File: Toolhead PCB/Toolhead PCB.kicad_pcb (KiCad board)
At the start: 2 copper layers, 35.7 x 22 mm, 9 parts, among them J1 PicoA, J2 PicoB, J3 PicoC, J4 Heater, J5 Thermistor, J6 Heatbreak Fan, J7 Part Fan, J8 IR+ADXL345, J9 MicroProbe

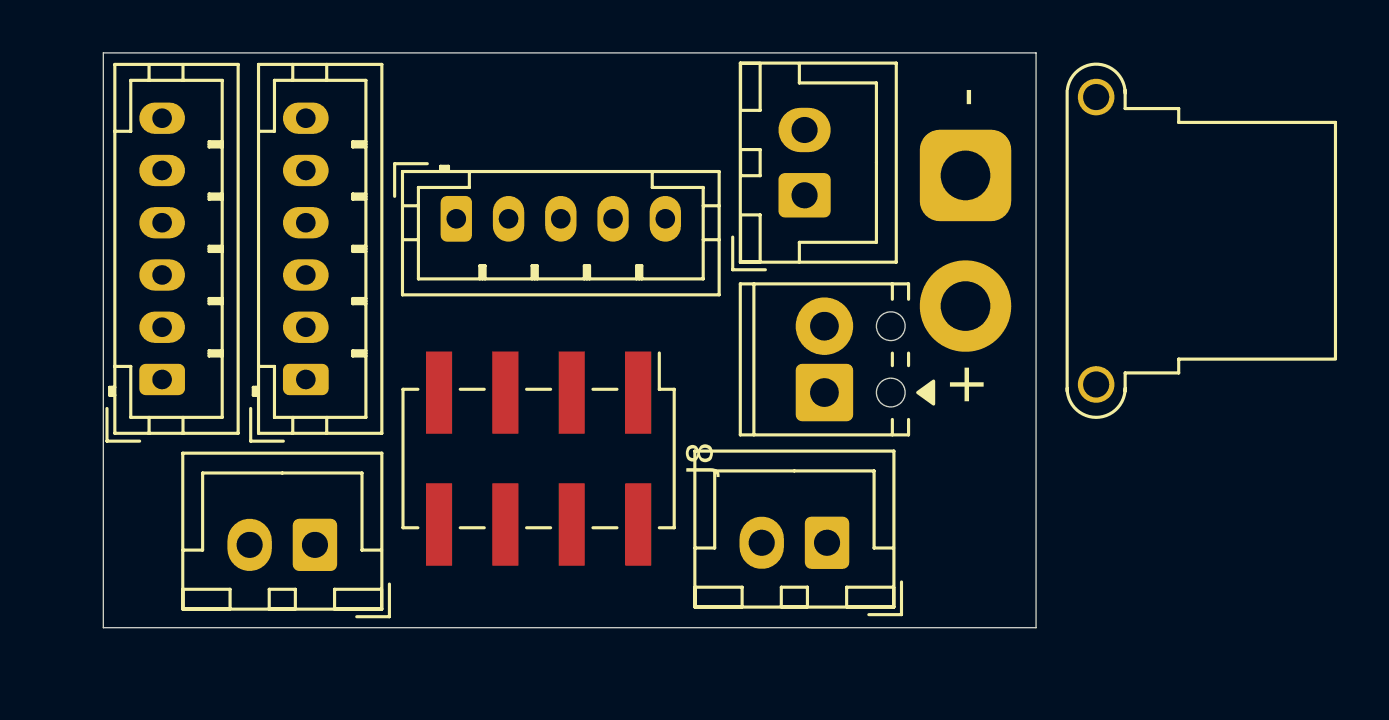
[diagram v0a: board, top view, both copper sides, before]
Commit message: Used wider traces for heater, fans, thermistor, microprobe power, etc.
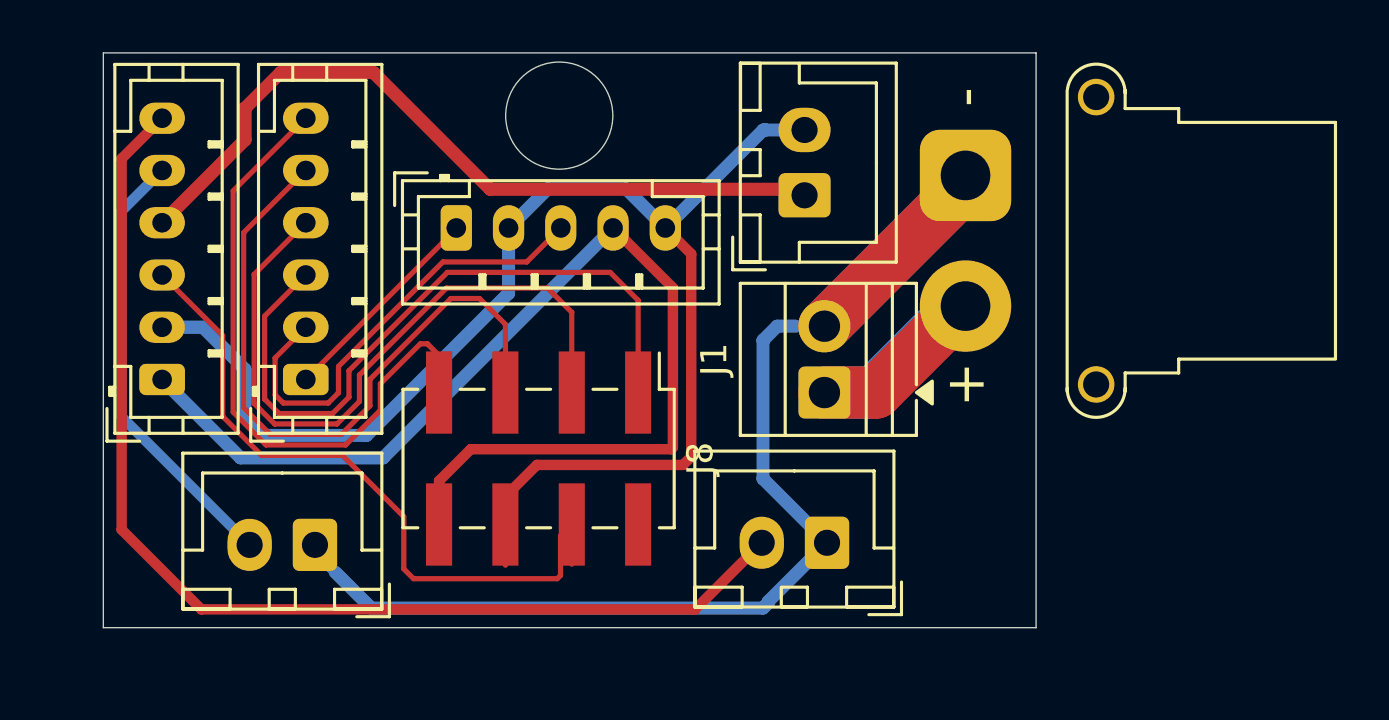
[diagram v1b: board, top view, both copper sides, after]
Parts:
- J1: footprint TerminalBlock_Phoenix:TerminalBlock_Phoenix_MPT-0,5-2-2.54_1x02_P2.54mm_Horizontal -> TerminalBlock:TerminalBlock_Xinya_XY308-2.54-2P_1x02_P2.54mm_Horizontal
- moved J9 0.35 mm to (113.5, 56.7)
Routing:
- net Net-(J3-Pin_2): track 0.00 -> 56.2 mm
- net Net-(J1-Pin_2): track 0.00 -> 53.3 mm
- net Net-(J3-Pin_6): track 0.00 -> 47.3 mm
- net Net-(J3-Pin_1): track 0.00 -> 43.0 mm
- net Net-(J3-Pin_4): track 0.00 -> 30.2 mm
- net Net-(J3-Pin_3): track 0.00 -> 26.8 mm
- net Net-(J2-Pin_3): track 0.00 -> 26.7 mm
- net Net-(J2-Pin_4): track 0.00 -> 26.4 mm
- net Net-(J2-Pin_5): track 0.00 -> 26.3 mm
- net Net-(J2-Pin_6): track 0.00 -> 24.6 mm
- net Net-(J2-Pin_2): track 0.00 -> 17.5 mm
- net Net-(J3-Pin_5): track 0.00 -> 17.0 mm
- net Net-(J1-Pin_1): track 0.00 -> 14.8 mm
- net Net-(J2-Pin_1): track 0.00 -> 8.19 mm
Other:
- outline, holes or cut-outs redrawn

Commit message: Combine a through-hole and an SMD connector to get the passthrough holes and vias.
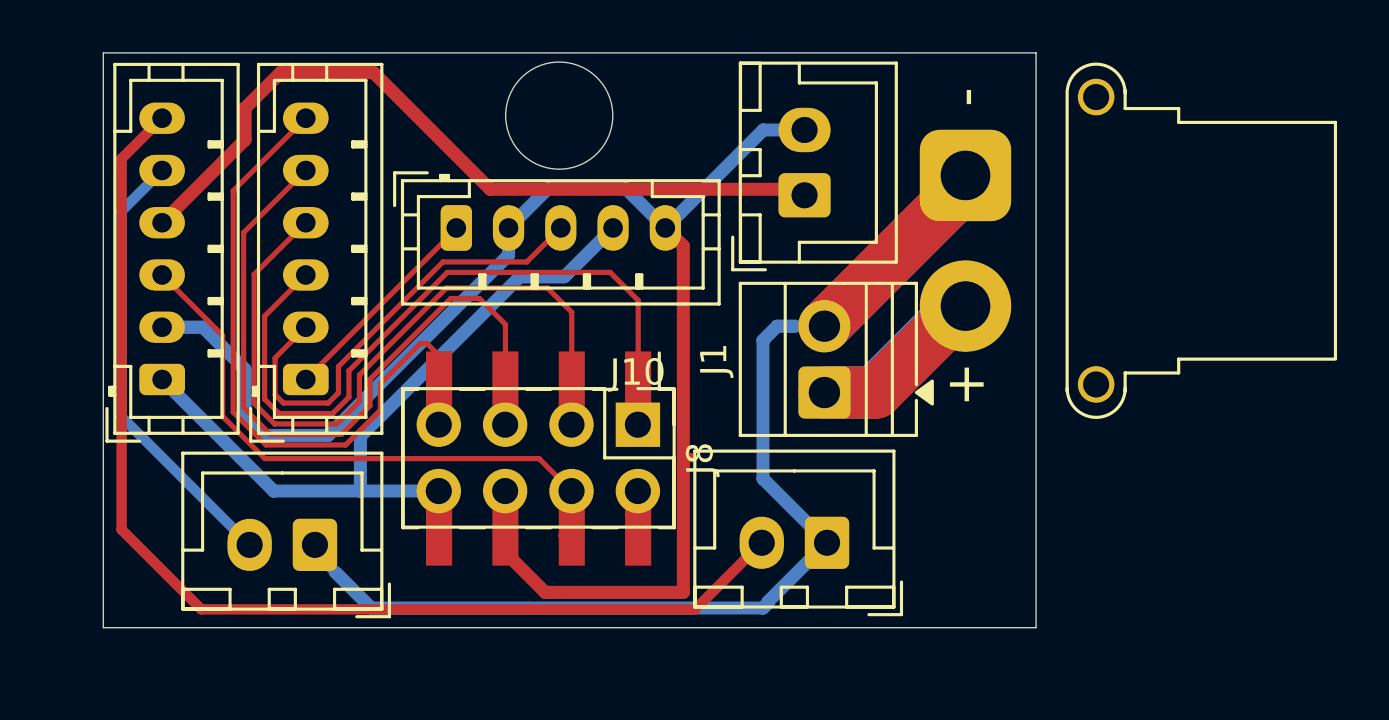
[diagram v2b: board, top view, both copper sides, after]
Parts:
- added J10: Conn_02x04_Odd_Even, Connector_PinHeader_2.54mm:PinHeader_2x04_P2.54mm_Vertical, F.Cu at (120.5, 64.2)
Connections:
- J8 pad 2: unconnected-(J8-Pin_2-Pad2) -> Net-(J10-Pin_2)
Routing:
- net Net-(J10-Pin_8): track 43.0 -> 30.0 mm
- net Net-(J10-Pin_4): track 26.8 -> 21.5 mm
- net Net-(J10-Pin_6): track 56.2 -> 59.2 mm

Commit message: JST connectors are soldered to the back: added 8 vias for signal and 2 vias for fan power. Added mounting holes (but have not resolved clearances).
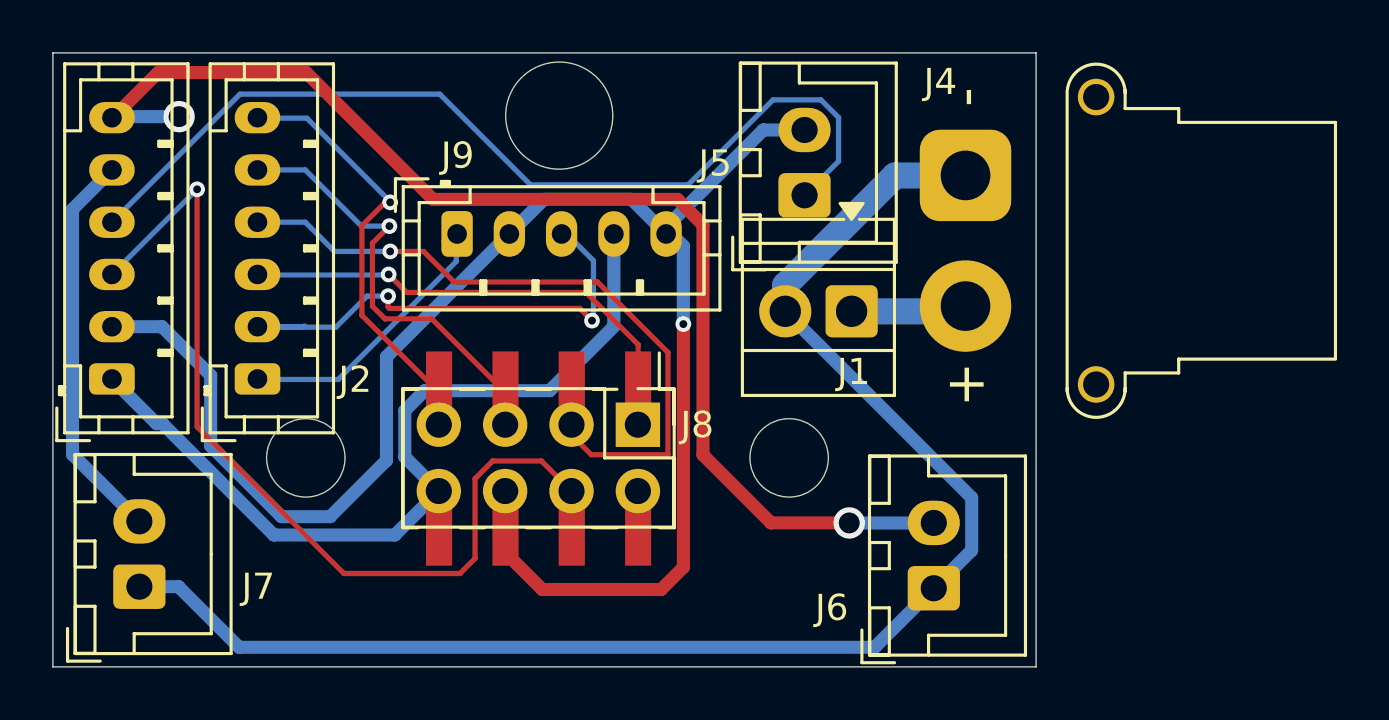
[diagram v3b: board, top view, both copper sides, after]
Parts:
- moved J7 6.91 mm to (101.4, 70.4), turned to 90 degrees
- moved J6 4.44 mm to (131.8, 70.5), turned to 90 degrees
- moved J1 3.28 mm to (128.6, 59.9), turned to 180 degrees
- moved J3 1.92 mm to (100.3, 62.5)
- moved J2 1.85 mm to (105.9, 62.5)
- moved J9 0.23 mm to (113.5, 56.9)
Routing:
- net Net-(J10-Pin_4): track 21.5 -> 34.8 mm, vias 0 -> 1
- net Net-(J1-Pin_1): track 14.8 -> 4.75 mm
- net Net-(J10-Pin_5): track 26.3 -> 17.1 mm, vias 0 -> 1
- net Net-(J10-Pin_1): track 26.7 -> 18.9 mm, vias 0 -> 1
- net Net-(J10-Pin_7): track 24.6 -> 16.9 mm, vias 0 -> 1
- net Net-(J3-Pin_4): track 30.2 -> 36.7 mm
- net Net-(J10-Pin_6): track 59.2 -> 64.9 mm, vias 0 -> 1
- net Net-(J10-Pin_8): track 30.0 -> 33.8 mm
- net Net-(J1-Pin_2): track 53.3 -> 56.8 mm
- net Net-(J2-Pin_1): track 8.19 -> 11.5 mm
- net Net-(J2-Pin_2): track 17.5 -> 19.8 mm, vias 0 -> 2
- net Net-(J3-Pin_5): track 17.0 -> 15.1 mm
- net Net-(J10-Pin_3): track 26.4 -> 27.3 mm, vias 0 -> 1
- net Net-(J3-Pin_6): track 47.3 -> 47.1 mm, vias 0 -> 2
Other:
- board size 35.7 x 22 mm -> 37.6 x 23.5 mm

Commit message: Holes for mounting. Moved traces to avoid holes. Moved most vias to the large pads. Changed the ADXLL345 wire order so it would route better. Made Schematic match PCB.
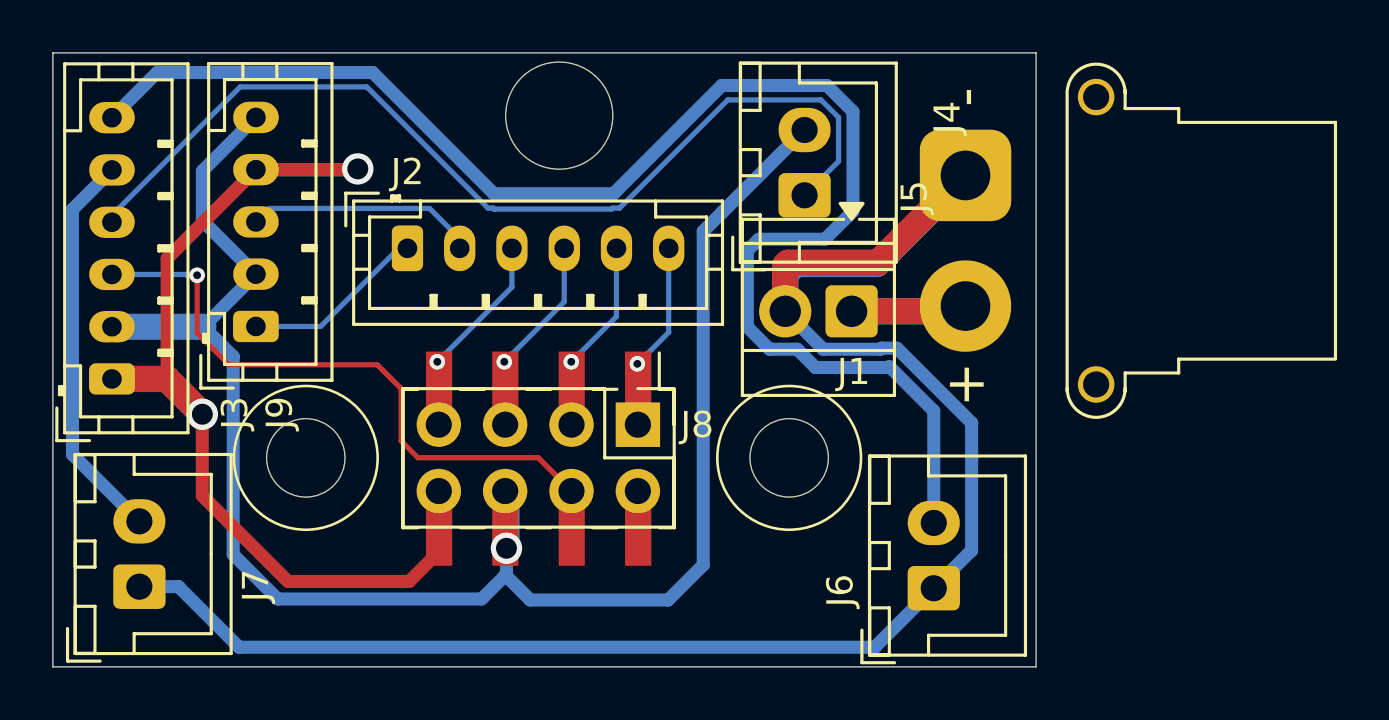
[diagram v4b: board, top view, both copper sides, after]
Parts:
- moved J9 8.47 mm to (105.8, 60.5), turned to 90 degrees
- moved J2 7.61 mm to (111.6, 57.5), turned to 0 degrees
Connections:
- J2 pad 3: Net-(J10-Pin_1) -> Net-(J10-Pin_7)
- J2 pad 4: Net-(J10-Pin_3) -> Net-(J10-Pin_5)
- J2 pad 5: Net-(J10-Pin_5) -> Net-(J10-Pin_3)
- J2 pad 6: Net-(J10-Pin_7) -> Net-(J10-Pin_1)
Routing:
- net Net-(J10-Pin_3): track 27.3 -> 7.46 mm
- net Net-(J10-Pin_1): track 18.9 -> 6.23 mm
- net Net-(J1-Pin_2): track 56.8 -> 68.9 mm
- net Net-(J10-Pin_4): track 34.8 -> 23.5 mm
- net Net-(J2-Pin_2): track 19.8 -> 8.86 mm, vias 2 -> 0
- net Net-(J3-Pin_6): track 47.1 -> 57.3 mm, vias 2 -> 0
- net Net-(J10-Pin_7): track 16.9 -> 7.66 mm
- net Net-(J10-Pin_6): track 64.9 -> 73.3 mm
- net Net-(J10-Pin_5): track 17.1 -> 8.91 mm
- net Net-(J10-Pin_8): track 33.8 -> 39.2 mm, vias 0 -> 2
- net Net-(J2-Pin_1): track 11.5 -> 7.04 mm
- net Net-(J1-Pin_1): track 4.75 -> 9.20 mm
- net Net-(J3-Pin_4): track 36.7 -> 37.9 mm

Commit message: Thicker traces for heater, fans, and shared ground or power.
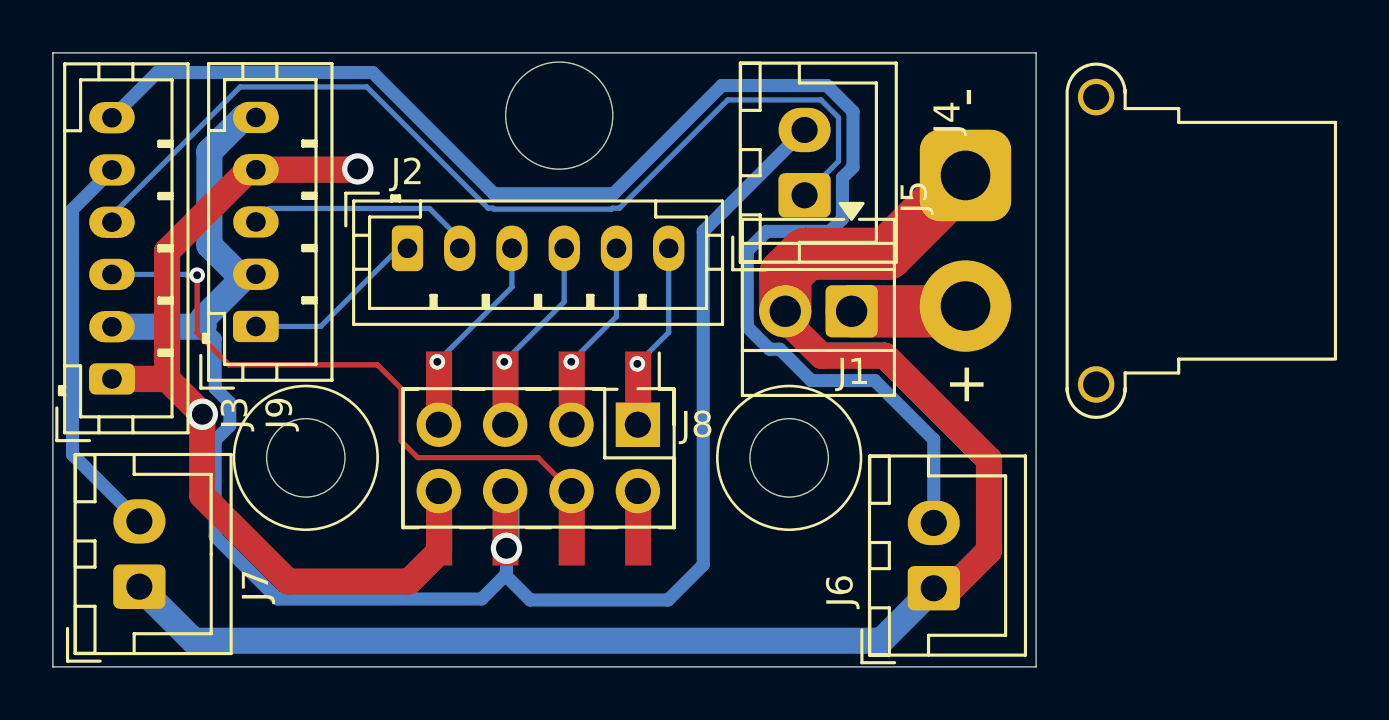
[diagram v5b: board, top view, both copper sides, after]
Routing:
- net Net-(J1-Pin_2): track 68.9 -> 85.7 mm
- net Net-(J10-Pin_8): track 39.2 -> 40.5 mm
- net Net-(J10-Pin_6): track 73.3 -> 74.4 mm
- net Net-(J3-Pin_6): track 57.3 -> 56.6 mm
